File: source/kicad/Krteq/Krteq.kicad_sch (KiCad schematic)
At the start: 254 parts, among them Q1 Q_NMOS_GSD, SW1 Switch, SW10 Switch, SW11 Switch, SW12 Switch, SW13 Switch, SW14 Switch, SW15 Switch, SW16 Switch, SW17 Switch, SW18 Switch, SW19 Switch, SW2 Switch, SW20 Switch, SW21 Switch, SW22 Switch, SW23 Switch, SW24 Switch, SW25 Switch, SW26 Switch, SW27 Switch, SW28 Switch, SW29 Switch, SW3 Switch, SW30 Switch, SW31 Switch, SW32 Switch, SW33 Switch, SW34 Switch, SW35 Switch, SW36 Switch, SW37 Switch, SW38 Switch, SW39 Switch, SW4 Switch, SW40 Switch, SW41 Switch, SW42 Switch, SW43 Switch, SW44 Switch, SW45 Switch, SW46 Switch, SW47 Switch, SW48 Switch, SW49 Switch, SW5 Switch, SW50 Switch, SW51 Switch, SW52 Switch, SW53 Switch, SW54 Switch, SW55 Switch, SW56 Switch, SW57 Switch, SW58 Switch, SW59 Switch, SW6 Switch, SW60 Switch, SW61 Switch, SW7 Switch, SW8 Switch, SW9 Switch

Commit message: case updates
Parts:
- D1, D2, D3: footprint LED_THT:LED_D3.0mm -> LED_THT:LED_D5.0mm
- SW1, SW10, SW11, SW12, SW13, SW14, SW15, SW16, SW17, SW18, SW19, SW2, SW20, SW21, SW22, SW23, SW24, SW25, SW26, SW27, SW28, SW29, SW3, SW30, SW32, SW33, SW34, SW35, SW36, SW37, SW38, SW39, SW4, SW40, SW41, SW42, SW43, SW44, SW45, SW46, SW47, SW48, SW49, SW5, SW50, SW51, SW52, SW53, SW54, SW55, SW56, SW57, SW58, SW59, SW6, SW60, SW61, SW7, SW8, SW9: value Switch -> Switch 1u
- SW31: value Switch -> Switch 2u
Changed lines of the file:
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@@
 			)
 		)
-		(property "Value" "Switch"
+		(property "Value" "Switch 1u"
 			(at 228.6 91.694 0)
 			(do_not_autoplace yes)
@@
 			)
 		)
-		(property "Value" "Switch"
+		(property "Value" "Switch 1u"
 			(at 215.9 57.404 0)
 			(do_not_autoplace yes)
@@
 			)
 		)
-		(property "Footprint" "LED_THT:LED_D3.0mm"
+		(property "Footprint" "LED_THT:LED_D5.0mm"
 			(at 76.2 191.77 0)
 			(effects
@@
 			)
 		)
-		(property "Value" "Switch"
+		(property "Value" "Switch 1u"
 			(at 279.4 57.404 0)
 			(do_not_autoplace yes)
@@
 			)
 		)
-		(property "Value" "Switch"
+		(property "Value" "Switch 1u"
 			(at 203.2 57.404 0)
 			(do_not_autoplace yes)
@@
 			)
 		)
-		(property "Value" "Switch"
+		(property "Value" "Switch 1u"
 			(at 304.8 91.694 0)
 			(do_not_autoplace yes)
@@
 			)
 		)
-		(property "Value" "Switch"
+		(property "Value" "Switch 1u"
 			(at 215.9 91.694 0)
 			(do_not_autoplace yes)
@@
 			)
 		)
-		(property "Value" "Switch"
+		(property "Value" "Switch 1u"
 			(at 203.2 68.834 0)
 			(do_not_autoplace yes)
@@
 			)
 		)
-		(property "Value" "Switch"
+		(property "Value" "Switch 1u"
 			(at 228.6 57.404 0)
 			(do_not_autoplace yes)
@@
 			)
 		)
-		(property "Value" "Switch"
+		(property "Value" "Switch 1u"
 			(at 279.4 68.834 0)
 			(do_not_autoplace yes)
@@
 			)
 		)
-		(property "Value" "Switch"
+		(property "Value" "Switch 1u"
 			(at 254 80.264 0)
 			(do_not_autoplace yes)
@@
 			)
 		)
-		(property "Value" "Switch"
+		(property "Value" "Switch 1u"
 			(at 241.3 68.834 0)
 			(do_not_autoplace yes)
@@
 			)
 		)
-		(property "Value" "Switch"
+		(property "Value" "Switch 2u"
 			(at 247.65 103.124 0)
 			(do_not_autoplace yes)
@@
 			)
 		)
-		(property "Value" "Switch"
+		(property "Value" "Switch 1u"
 			(at 241.3 91.694 0)
 			(do_not_autoplace yes)
@@
 			)
 		)
-		(property "Value" "Switch"
+		(property "Value" "Switch 1u"
 			(at 292.1 68.834 0)
 			(do_not_autoplace yes)
@@
 			)
 		)
-		(property "Value" "Switch"
+		(property "Value" "Switch 1u"
 			(at 317.5 57.404 0)
 			(do_not_autoplace yes)
@@
 			)
 		)
-		(property "Value" "Switch"
+		(property "Value" "Switch 1u"
 			(at 304.8 57.404 0)
 			(do_not_autoplace yes)
@@
 			)
 		)
-		(property "Value" "Switch"
+		(property "Value" "Switch 1u"
 			(at 317.5 45.974 0)
 			(do_not_autoplace yes)
@@
 			)
 		)
-		(property "Value" "Switch"
+		(property "Value" "Switch 1u"
 			(at 304.8 103.124 0)
 			(do_not_autoplace yes)
@@
 			)
 		)
-		(property "Value" "Switch"
+		(property "Value" "Switch 1u"
 			(at 215.9 68.834 0)
 			(do_not_autoplace yes)
@@
 			)
 		)
-		(property "Footprint" "LED_THT:LED_D3.0mm"
+		(property "Footprint" "LED_THT:LED_D5.0mm"
 			(at 76.2 200.66 0)
 			(effects
@@
 			)
 		)
-		(property "Value" "Switch"
+		(property "Value" "Switch 1u"
 			(at 292.1 57.404 0)
 			(do_not_autoplace yes)
@@
 			)
 		)
-		(property "Value" "Switch"
+		(property "Value" "Switch 1u"
 			(at 228.6 68.834 0)
 			(do_not_autoplace yes)
@@
 			)
 		)
-		(property "Value" "Switch"
+		(property "Value" "Switch 1u"
 			(at 292.1 80.264 0)
 			(do_not_autoplace yes)
@@
 			)
 		)
-		(property "Footprint" "LED_THT:LED_D3.0mm"
+		(property "Footprint" "LED_THT:LED_D5.0mm"
 			(at 76.2 209.55 0)
 			(effects
@@
 			)
 		)
-		(property "Value" "Switch"
+		(property "Value" "Switch 1u"
 			(at 266.7 80.264 0)
 			(do_not_autoplace yes)
@@
 			)
 		)
-		(property "Value" "Switch"
+		(property "Value" "Switch 1u"
 			(at 215.9 80.264 0)
 			(do_not_autoplace yes)
@@
 			)
 		)
-		(property "Value" "Switch"
+		(property "Value" "Switch 1u"
 			(at 190.5 80.264 0)
 			(do_not_autoplace yes)
@@
 			)
 		)
-		(property "Value" "Switch"
+		(property "Value" "Switch 1u"
 			(at 279.4 91.694 0)
 			(do_not_autoplace yes)
@@
 			)
 		)
-		(property "Value" "Switch"
+		(property "Value" "Switch 1u"
 			(at 190.5 103.124 0)
 			(do_not_autoplace yes)
@@
 			)
 		)
-		(property "Value" "Switch"
+		(property "Value" "Switch 1u"
 			(at 279.4 103.124 0)
 			(do_not_autoplace yes)
@@
 			)
 		)
-		(property "Value" "Switch"
+		(property "Value" "Switch 1u"
 			(at 266.7 57.404 0)
 			(do_not_autoplace yes)
@@
 			)
 		)
-		(property "Value" "Switch"
+		(property "Value" "Switch 1u"
 			(at 241.3 57.404 0)
 			(do_not_autoplace yes)
@@
 			)
 		)
-		(property "Value" "Switch"
+		(property "Value" "Switch 1u"
 			(at 215.9 103.124 0)
 			(do_not_autoplace yes)
@@
 			)
 		)
-		(property "Value" "Switch"
+		(property "Value" "Switch 1u"
 			(at 254 68.834 0)
 			(do_not_autoplace yes)
@@
 			)
 		)
-		(property "Value" "Switch"
+		(property "Value" "Switch 1u"
 			(at 266.7 103.124 0)
 			(do_not_autoplace yes)
@@
 			)
 		)
-		(property "Value" "Switch"
+		(property "Value" "Switch 1u"
 			(at 177.8 91.694 0)
 			(do_not_autoplace yes)
@@
 			)
 		)
-		(property "Value" "Switch"
+		(property "Value" "Switch 1u"
 			(at 266.7 91.694 0)
 			(do_not_autoplace yes)
@@
 			)
 		)
-		(property "Value" "Switch"
+		(property "Value" "Switch 1u"
 			(at 292.1 103.124 0)
 			(do_not_autoplace yes)
@@
 			)
 		)
-		(property "Value" "Switch"
+		(property "Value" "Switch 1u"
 			(at 228.6 103.124 0)
 			(do_not_autoplace yes)
@@
 			)
 		)
-		(property "Value" "Switch"
+		(property "Value" "Switch 1u"
 			(at 266.7 68.834 0)
 			(do_not_autoplace yes)
@@
 			)
 		)
-		(property "Value" "Switch"
+		(property "Value" "Switch 1u"
 			(at 203.2 91.694 0)
 			(do_not_autoplace yes)
@@
 			)
 		)
-		(property "Value" "Switch"
+		(property "Value" "Switch 1u"
 			(at 254 91.694 0)
 			(do_not_autoplace yes)
@@
 			)
 		)
-		(property "Value" "Switch"
+		(property "Value" "Switch 1u"
 			(at 177.8 80.264 0)
 			(do_not_autoplace yes)
@@
 			)
 		)
-		(property "Value" "Switch"
+		(property "Value" "Switch 1u"
 			(at 177.8 45.974 0)
 			(do_not_autoplace yes)
@@
 			)
 		)
-		(property "Value" "Switch"
+		(property "Value" "Switch 1u"
 			(at 177.8 57.404 0)
 			(do_not_autoplace yes)
@@
 			)
 		)
-		(property "Value" "Switch"
+		(property "Value" "Switch 1u"
 			(at 292.1 91.694 0)
 			(do_not_autoplace yes)
@@
 			)
 		)
-		(property "Value" "Switch"
+		(property "Value" "Switch 1u"
 			(at 228.6 80.264 0)
 			(do_not_autoplace yes)
@@
 			)
 		)
-		(property "Value" "Switch"
+		(property "Value" "Switch 1u"
 			(at 241.3 80.264 0)
 			(do_not_autoplace yes)
@@
 			)
 		)
-		(property "Value" "Switch"
+		(property "Value" "Switch 1u"
 			(at 254 57.404 0)
 			(do_not_autoplace yes)
@@
 			)
 		)
-		(property "Value" "Switch"
+		(property "Value" "Switch 1u"
 			(at 190.5 68.834 0)
 			(do_not_autoplace yes)
@@
 			)
 		)
-		(property "Value" "Switch"
+		(property "Value" "Switch 1u"
 			(at 304.8 68.834 0)
 			(do_not_autoplace yes)
@@
 			)
 		)
-		(property "Value" "Switch"
+		(property "Value" "Switch 1u"
 			(at 317.5 68.834 0)
 			(do_not_autoplace yes)
@@
 			)
 		)
-		(property "Value" "Switch"
+		(property "Value" "Switch 1u"
 			(at 203.2 103.124 0)
 			(do_not_autoplace yes)
@@
 			)
 		)
-		(property "Value" "Switch"
+		(property "Value" "Switch 1u"
 			(at 317.5 103.124 0)
 			(do_not_autoplace yes)
@@
 			)
 		)
-		(property "Value" "Switch"
+		(property "Value" "Switch 1u"
 			(at 190.5 57.404 0)
 			(do_not_autoplace yes)
@@
 			)
 		)
-		(property "Value" "Switch"
+		(property "Value" "Switch 1u"
 			(at 317.5 80.264 0)
 			(do_not_autoplace yes)
@@
 			)
 		)
-		(property "Value" "Switch"
+		(property "Value" "Switch 1u"
 			(at 203.2 80.264 0)
 			(do_not_autoplace yes)
@@
 			)
 		)
-		(property "Value" "Switch"
+		(property "Value" "Switch 1u"
 			(at 190.5 91.694 0)
 			(do_not_autoplace yes)
@@
 			)
 		)
-		(property "Value" "Switch"
+		(property "Value" "Switch 1u"
 			(at 177.8 68.834 0)
 			(do_not_autoplace yes)
@@
 			)
 		)
-		(property "Value" "Switch"
+		(property "Value" "Switch 1u"
 			(at 177.8 103.124 0)
 			(do_not_autoplace yes)
@@
 			)
 		)
-		(property "Value" "Switch"
+		(property "Value" "Switch 1u"
 			(at 317.5 91.694 0)
 			(do_not_autoplace yes)
@@
 			)
 		)
-		(property "Value" "Switch"
+		(property "Value" "Switch 1u"
 			(at 304.8 80.264 0)
 			(do_not_autoplace yes)
@@
 			)
 		)
-		(property "Value" "Switch"
+		(property "Value" "Switch 1u"
 			(at 279.4 80.264 0)
 			(do_not_autoplace yes)

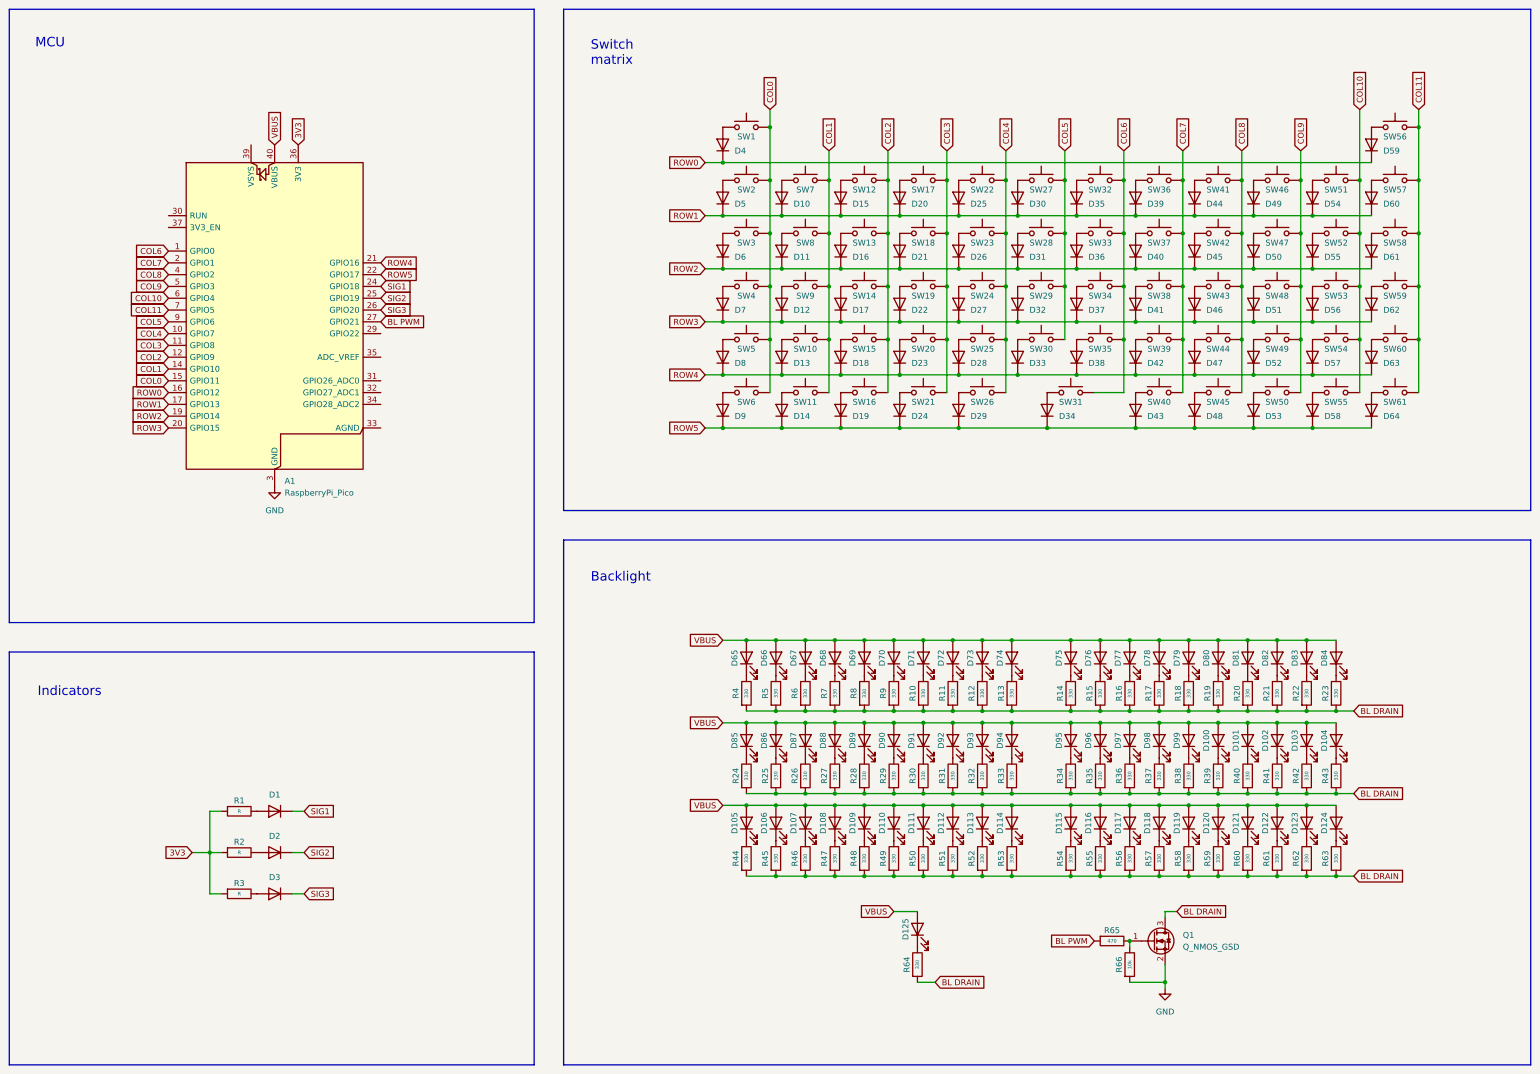
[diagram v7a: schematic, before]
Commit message: pcb placement
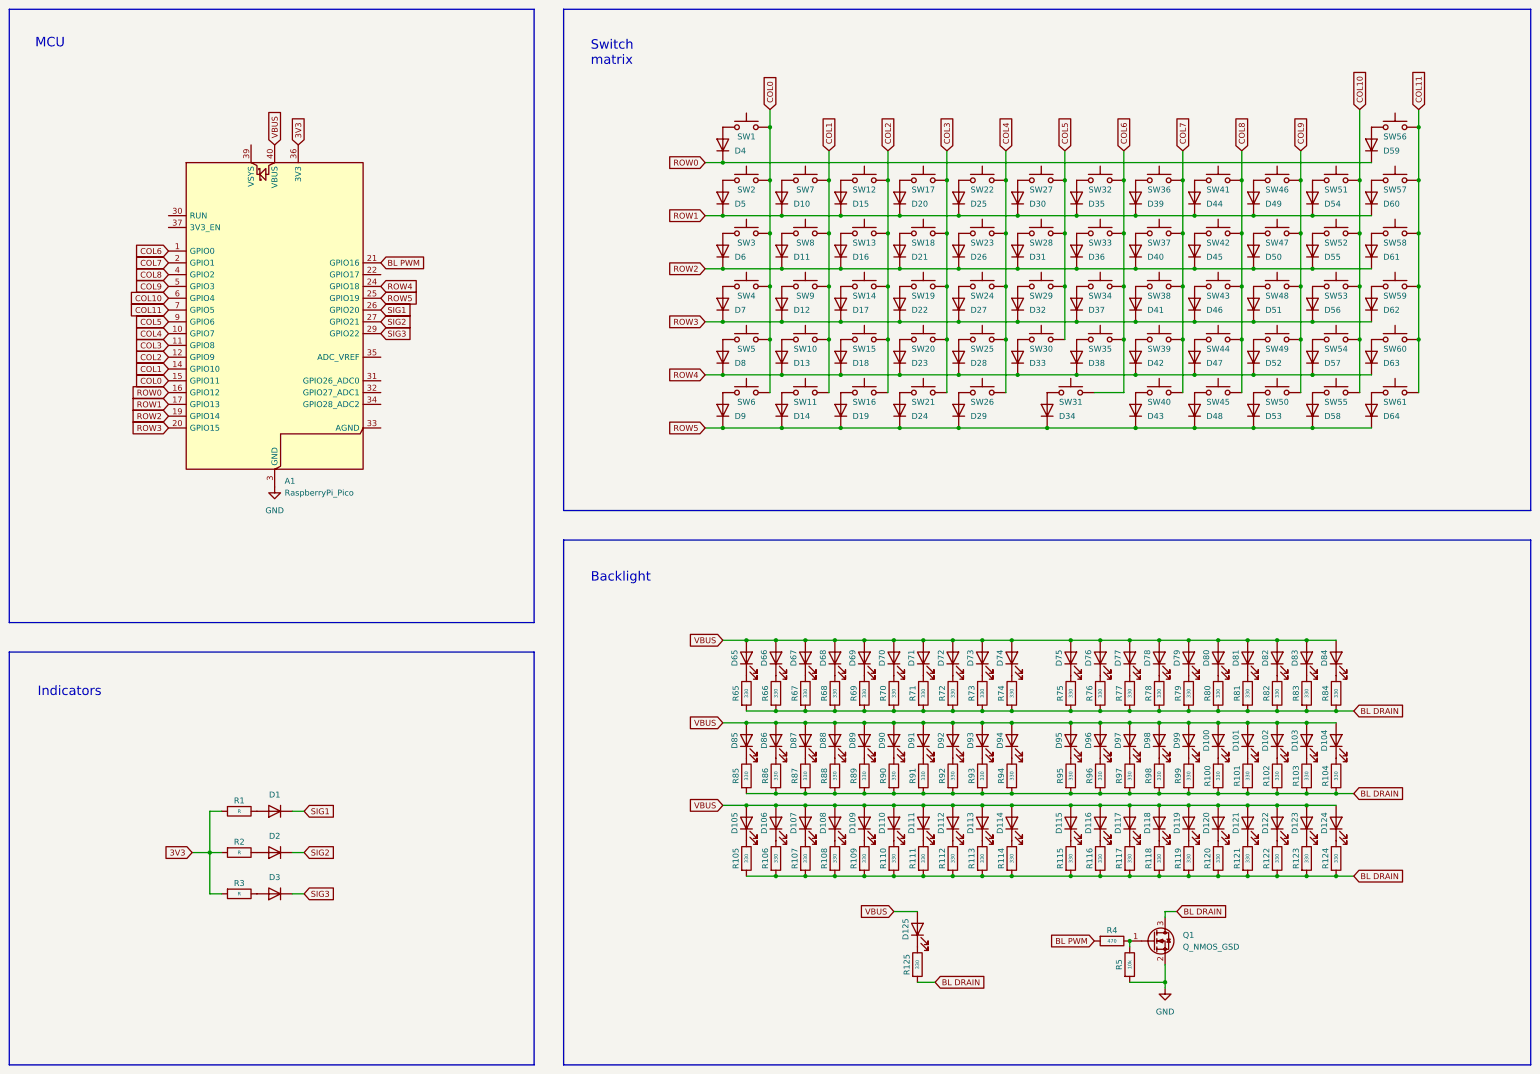
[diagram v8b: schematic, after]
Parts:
- renumbered R39 to R100, R40 to R101, R41 to R102, R42 to R103, R43 to R104, R44 to R105, R45 to R106, R46 to R107, R47 to R108, R48 to R109, R49 to R110, R50 to R111, R51 to R112, R52 to R113, R53 to R114, R54 to R115, R55 to R116, R56 to R117, R57 to R118, R58 to R119, R59 to R120, R60 to R121, R61 to R122, R62 to R123, R63 to R124, R64 to R125, R65 to R4, R66 to R5, R4 to R65, R5 to R66, R6 to R67, R7 to R68, R8 to R69, R9 to R70, R10 to R71, R11 to R72, R12 to R73, R13 to R74, R14 to R75, R15 to R76, R16 to R77, R17 to R78, R18 to R79, R19 to R80, R20 to R81, R21 to R82, R22 to R83, R23 to R84, R24 to R85, R25 to R86, R26 to R87, R27 to R88, R28 to R89, R29 to R90, R30 to R91, R31 to R92, R32 to R93, R33 to R94, R34 to R95, R35 to R96, R36 to R97, R37 to R98, R38 to R99
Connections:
- net BL PWM: now also A1.21 (GPIO16); no longer A1.27 (GPIO21)
- net ROW4: now also A1.24 (GPIO18); no longer A1.21 (GPIO16)
- net ROW5: now also A1.25 (GPIO19); no longer A1.22 (GPIO17)
- net SIG1: now also A1.26 (GPIO20); no longer A1.24 (GPIO18)
- net SIG2: now also A1.27 (GPIO21); no longer A1.25 (GPIO19)
- net SIG3: now also A1.29 (GPIO22); no longer A1.26 (GPIO20)
